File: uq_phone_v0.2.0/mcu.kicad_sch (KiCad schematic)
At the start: 41 parts, among them J6 Conn_ARM_SWD_TagConnect_TC2030, J7 559092474, J9 559092474, Q1 MMBT3904LP-7, Q2 MMBT3904LP-7, U17 TXU0204DTRR, U18 TXU0304DTRR, U19 TXU0104DTRR, U20 TXU0104DTRR, U5 TCA9509MRVHR, U6 STM32H723VGHx

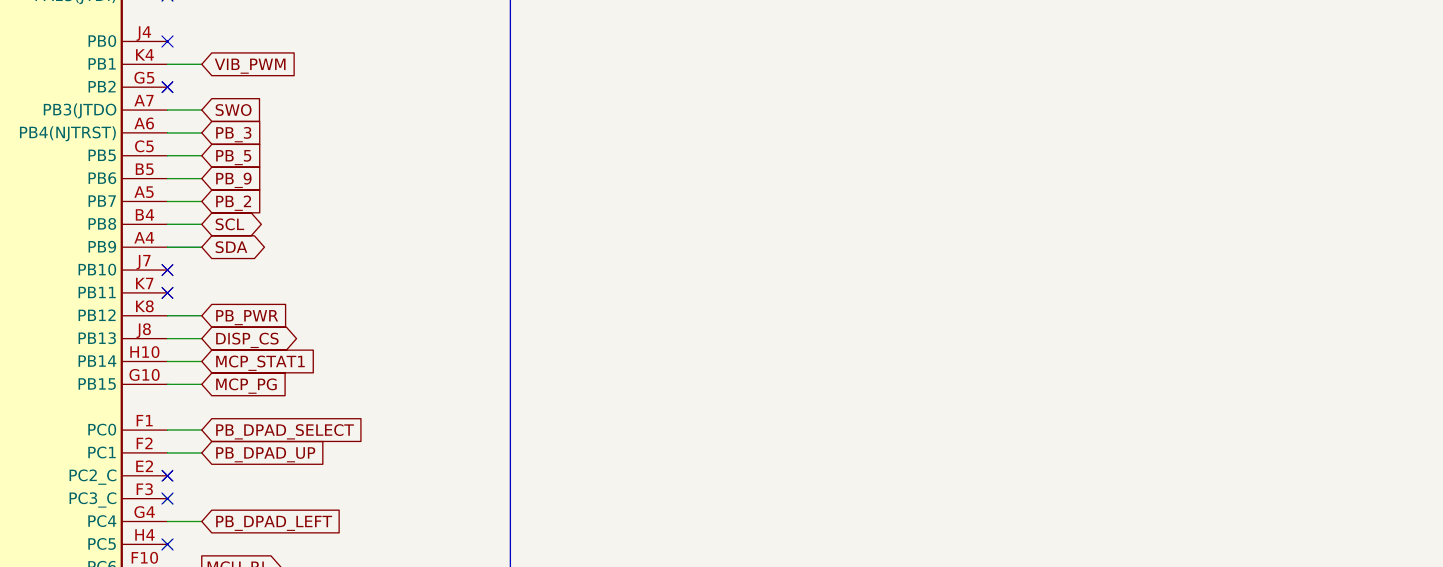
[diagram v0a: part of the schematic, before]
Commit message: Implement D-1 MicroSD load switch
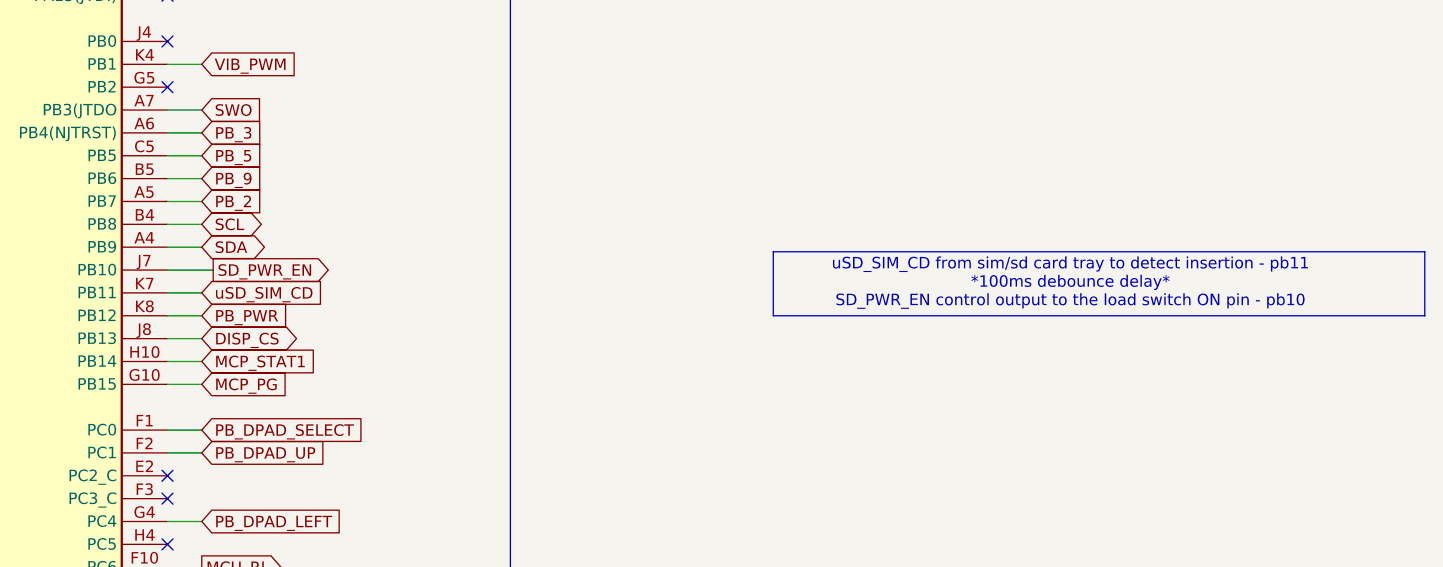
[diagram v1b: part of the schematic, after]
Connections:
- net SD_PWR_EN: now reaches U6.J7 (PB10)
- net uSD_SIM_CD: now reaches U6.K7 (PB11)
- no-connect marks 18 -> 16
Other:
- note added: "uSD_SIM_CD from sim/sd card tray to detect insertion - pb11 *100ms debounce delay* SD_PWR_EN control output to the load switch ON pin - pb10"
